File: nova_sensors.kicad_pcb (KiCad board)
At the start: 2 copper layers, 100 x 82.5 mm, 93 parts, among them J1 Conn_01x03_Socket, J10 Conn_01x04_Socket, J11 Conn_01x04_Socket, J2 Conn_01x03_Socket, J3 Conn_01x04_Socket, J4 Conn_01x02_Socket, J5 Conn_01x02_Socket, J6 Conn_01x03_Socket, J7 Conn_01x02_Socket, J8 Conn_01x02_Socket, J9 Conn_01x02_Socket, SW1 SW_Push, SW2 SW_DIP_x02, SW3 SW_DIP_x02, U1 AT32F455CET7, U2 MAX3232, U3 MAX13488, U4 MAX13488, U5 LD1117S33TR, U6 XL1509-ADJ, Y1 8Mhz, Y2 32768hz

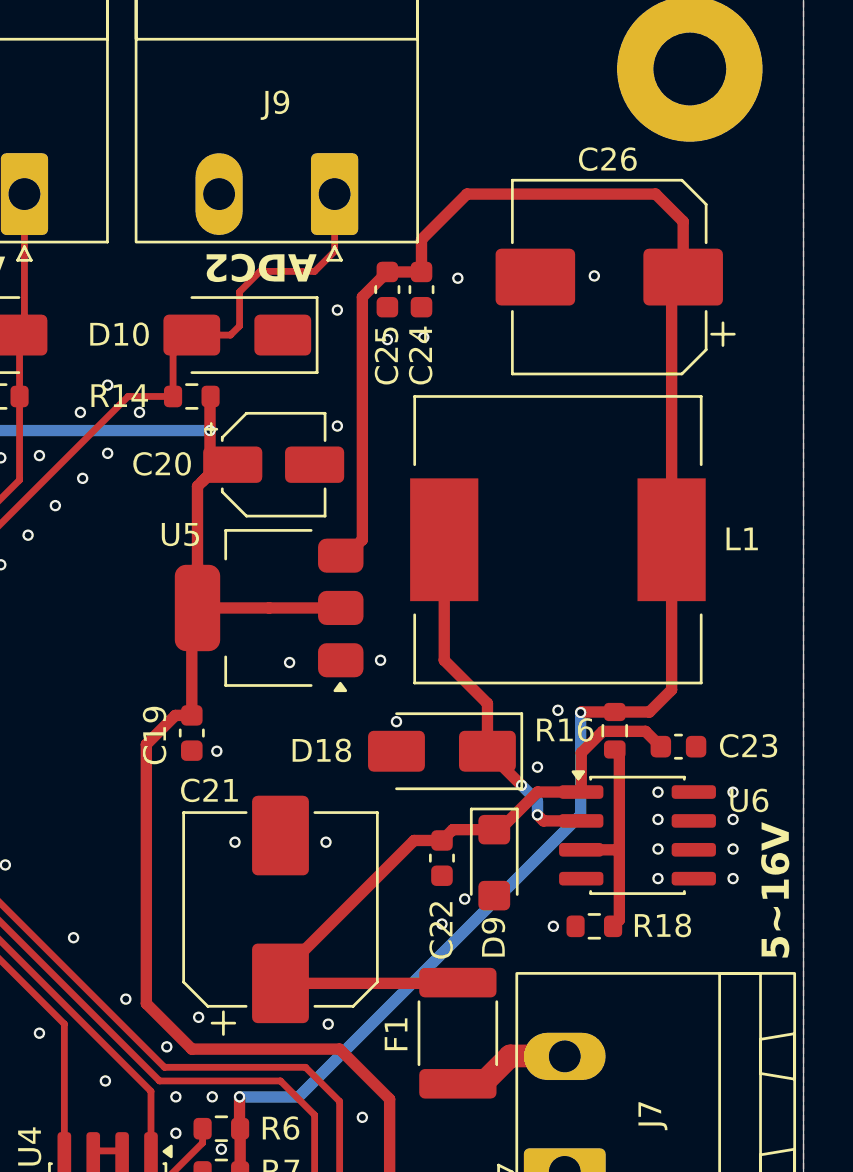
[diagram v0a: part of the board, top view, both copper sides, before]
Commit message: fix: 调整贴片铝解电容的封装大小
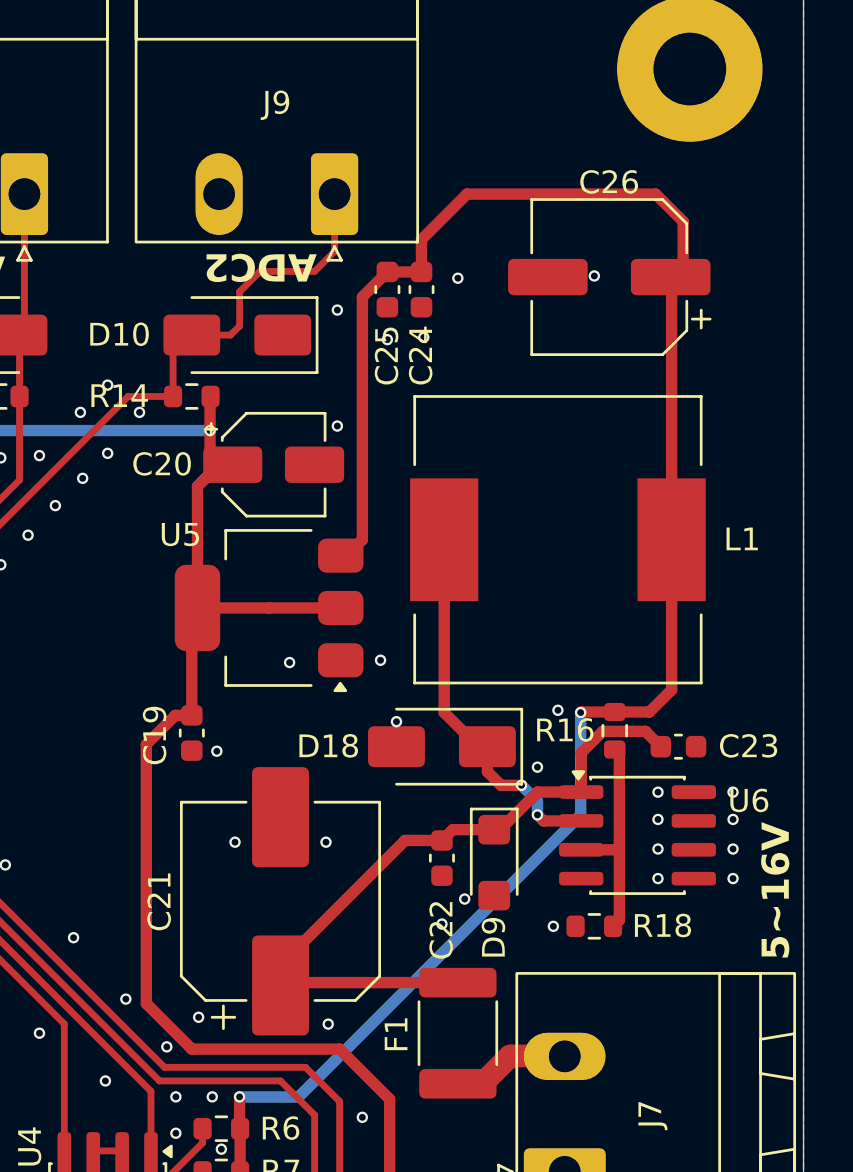
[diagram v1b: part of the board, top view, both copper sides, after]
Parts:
- C21: footprint Capacitor_SMD:CP_Elec_8x10 -> Capacitor_SMD:CP_Elec_8x10.5
- C26: footprint Capacitor_SMD:CP_Elec_8x10 -> Capacitor_SMD:CP_Elec_6.3x7.7
- moved C21 0.36 mm to (77.0, 169.1)
- moved D18 0.20 mm to (84.1, 162.3)
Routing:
- net Net-(D18-K): track 15.8 -> 16.6 mm
